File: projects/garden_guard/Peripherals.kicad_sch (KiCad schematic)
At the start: 13 parts, among them J1 Conn_02x05_Odd_Even, J6 Conn_02x06_Odd_Even, J8 Conn_02x01, J9 Conn_02x01, U10 DMN2028USS-13, U11 DMN2028USS-13

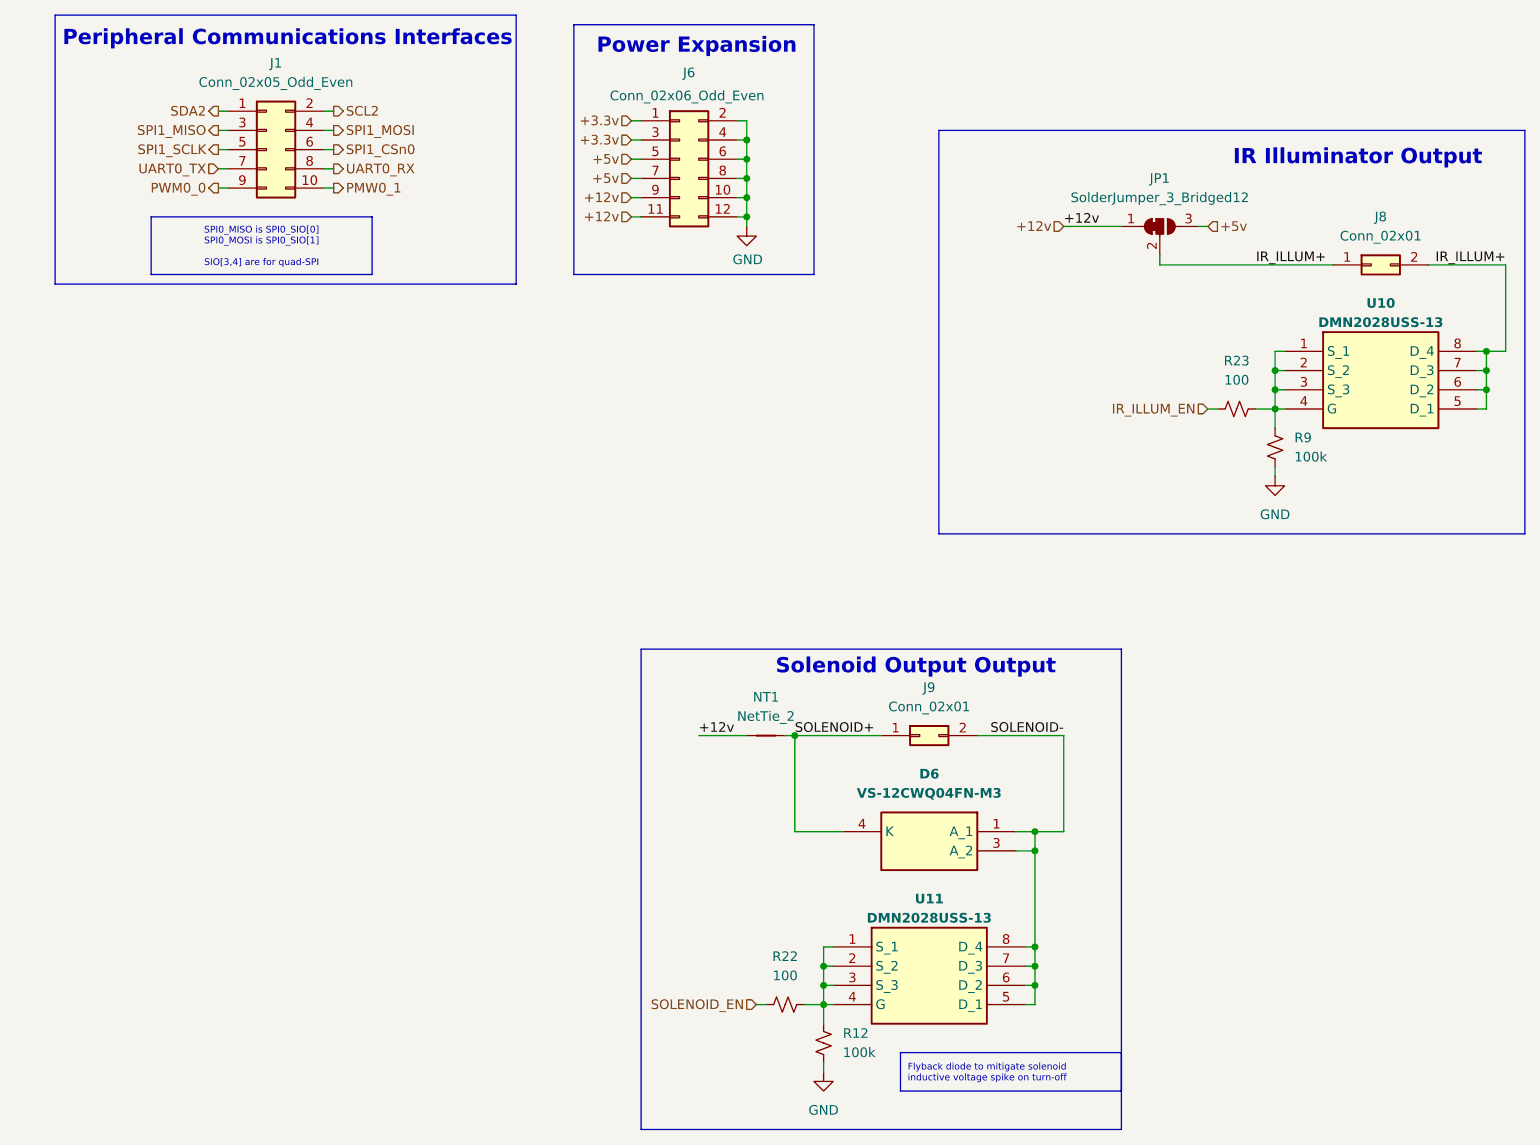
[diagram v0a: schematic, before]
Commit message: - Add all missing footprints - Add specific part numbers to each component in schematic
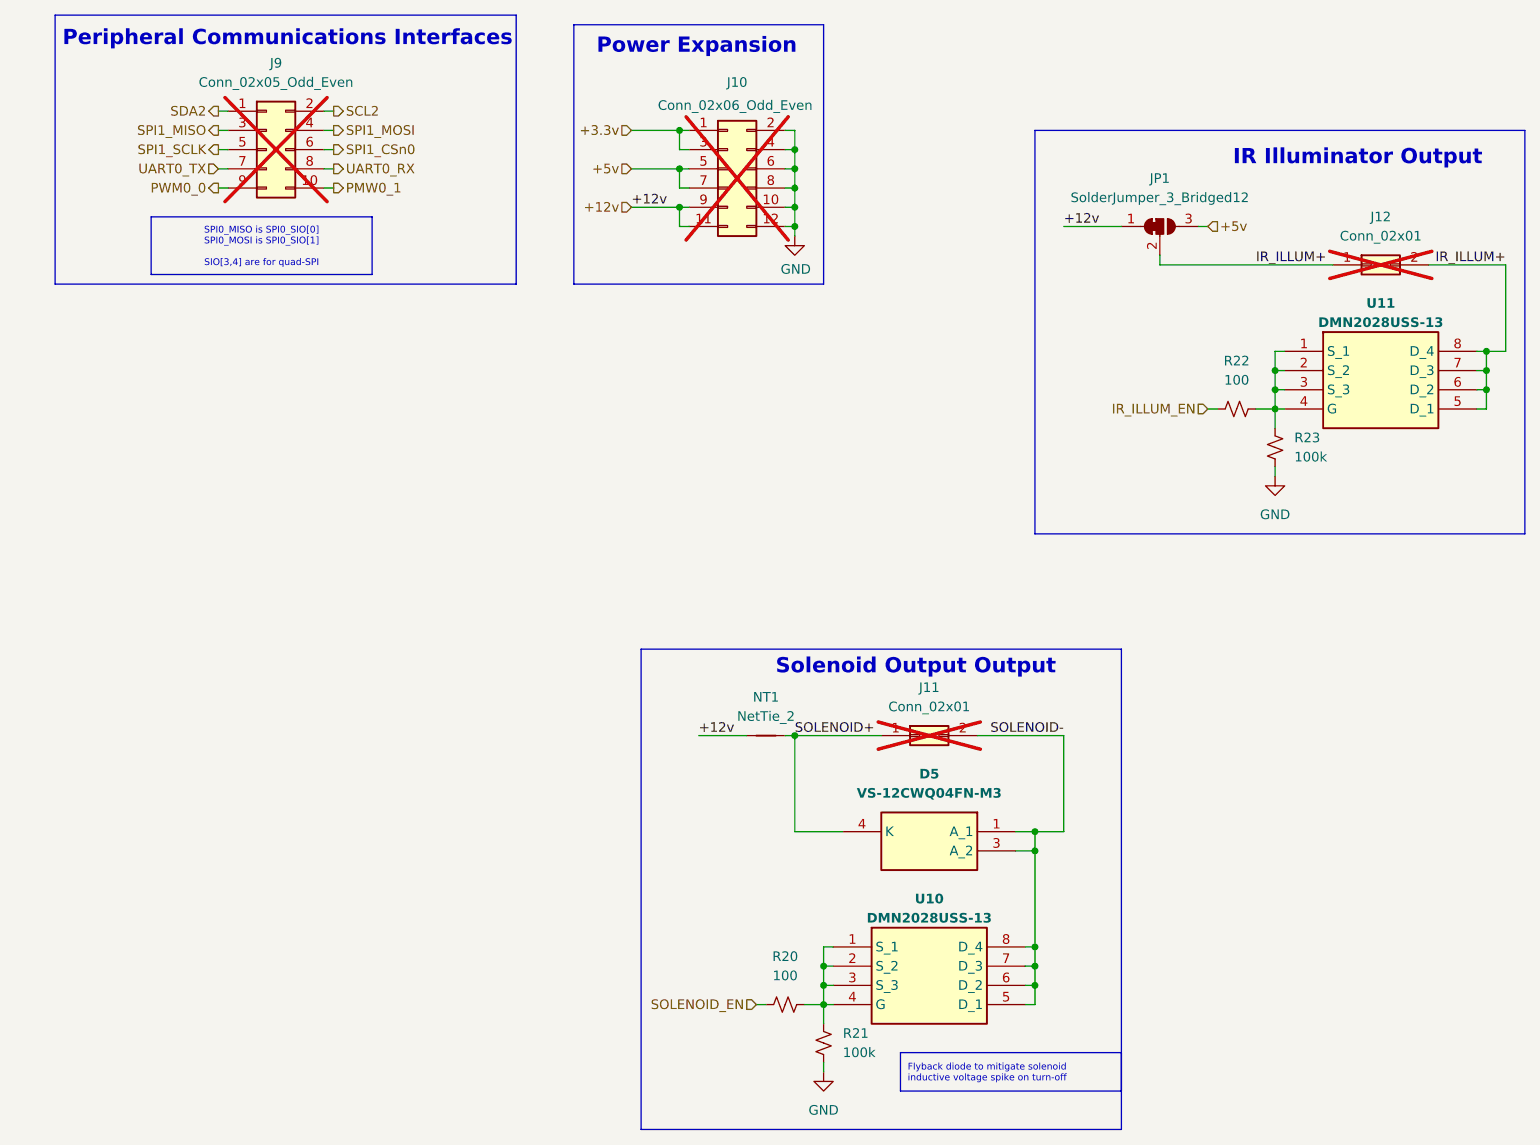
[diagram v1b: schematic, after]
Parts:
- removed J9: Conn_02x01, symbol Connector_Generic:Conn_02x01
- removed R9: 100k, symbol Device:R_Small_US
- added J11: Conn_02x01, Connector_PinHeader_2.54mm:PinHeader_1x02_P2.54mm_Vertical, symbol Connector_Generic:Conn_02x01
- added R23: 100k, Resistor_SMD:R_0603_1608Metric, symbol Device:R_Small_US
- J10: renamed from J6; footprint (none) -> Connector_PinHeader_2.54mm:PinHeader_2x06_P2.54mm_Vertical; now not fitted; now left out of the parts list
- J12: renamed from J8; footprint (none) -> Connector_PinHeader_2.54mm:PinHeader_1x02_P2.54mm_Vertical; now not fitted; now left out of the parts list
- J9: renamed from J1; footprint (none) -> Connector_PinHeader_2.54mm:PinHeader_2x05_P2.54mm_Vertical; now not fitted; now left out of the parts list
- JP1: footprint (none) -> Jumper:SolderJumper-3_P1.3mm_Bridged12_RoundedPad1.0x1.5mm
- NT1: footprint (none) -> NetTie:NetTie-2_SMD_Pad0.5mm
- R20: renamed from R22; footprint (none) -> Resistor_SMD:R_0603_1608Metric
- R21: renamed from R12; footprint (none) -> Resistor_SMD:R_0603_1608Metric; MPN (none) -> RC0603FR-07100KL; Mfr (none) -> YAGEO
- R22: renamed from R23; footprint (none) -> Resistor_SMD:R_0603_1608Metric
- renumbered D6 to D5, U11 to U10, U10 to U11
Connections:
- net GND: now also R23.2
- net SOLENOID+: now also J11.1 (Pin_1)
- net SOLENOID-: now also J11.2 (Pin_2)
- net at R22.2, U11.1 (S_1), U11.2 (S_2)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: now also R23.1

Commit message: - Find part numbers for CM5 parts - Minor CM5 symbol, footprint adjustments - Move to uniform small resistor and capacitor symbols - Add *lck to .gitignore
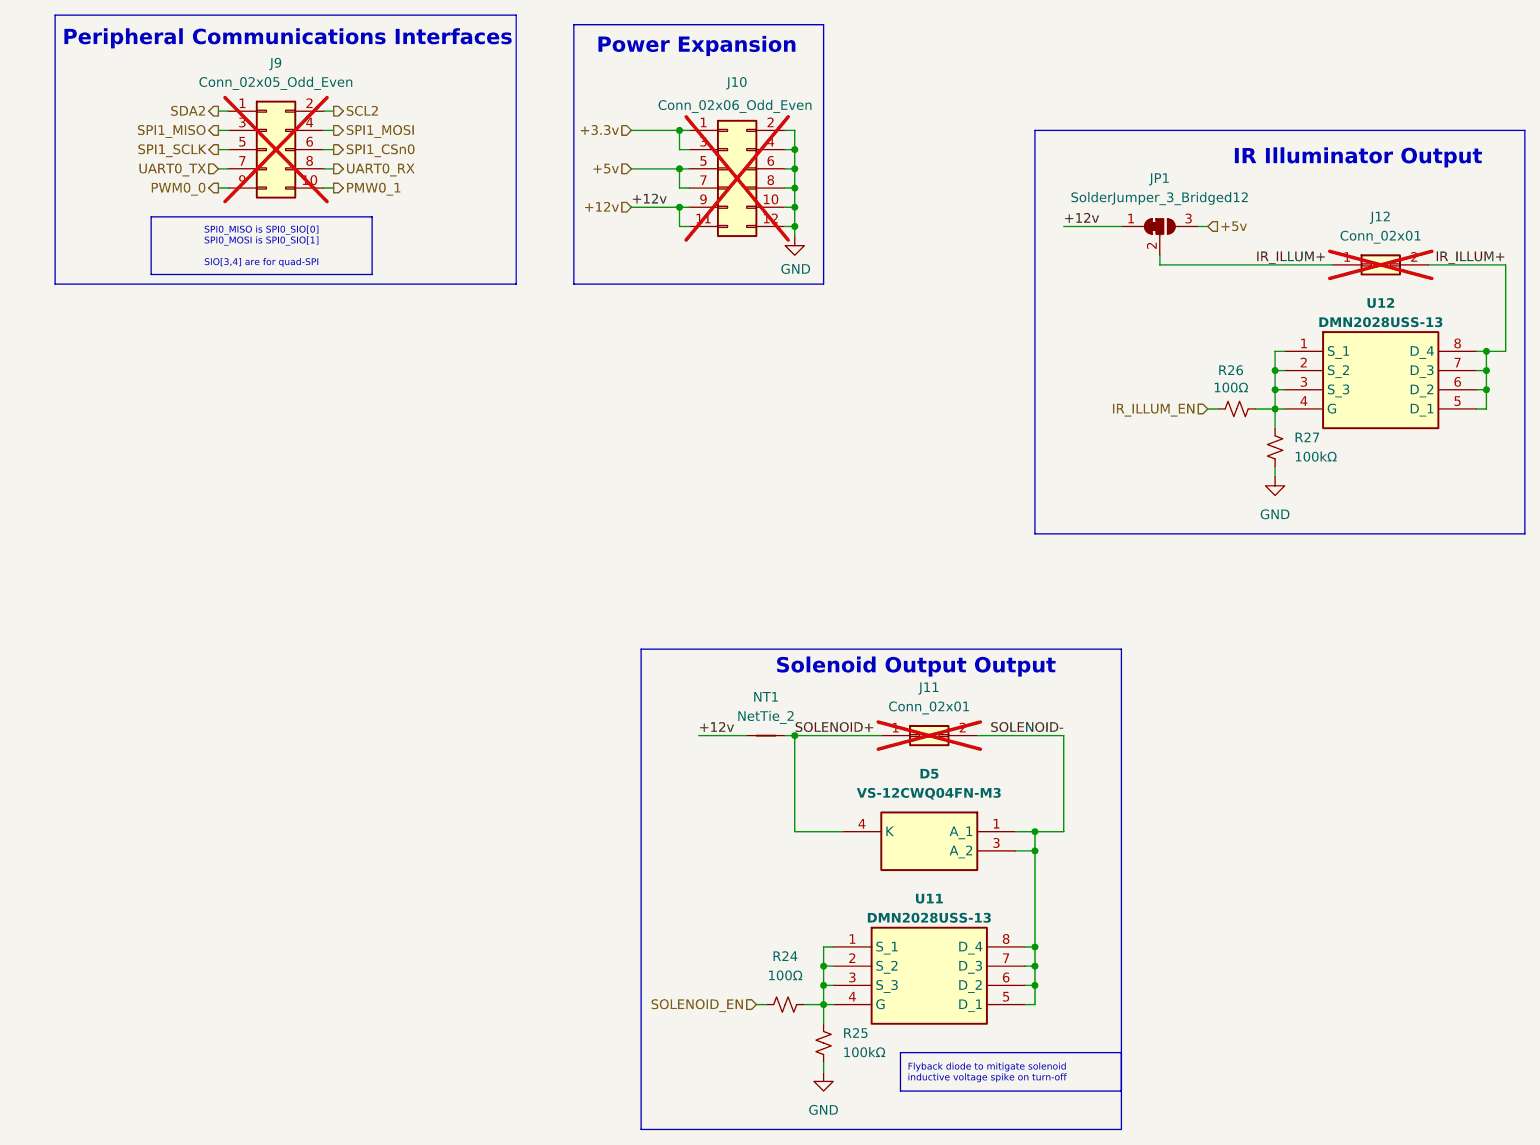
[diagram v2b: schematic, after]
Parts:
- removed R22: 100, Resistor_SMD:R_0603_1608Metric, symbol Device:R_Small_US
- removed R23: 100k, Resistor_SMD:R_0603_1608Metric, symbol Device:R_Small_US
- added R26: 100Ω, Resistor_SMD:R_0603_1608Metric, symbol Device:R_Small_US
- added R27: 100kΩ, Resistor_SMD:R_0603_1608Metric, symbol Device:R_Small_US
- D5: MPN (none) -> VS-12CWQ04FN-M3; Mfr (none) -> Vishay
- R24: renamed from R20; value 100 -> 100Ω; MPN (none) -> RC0603FR-07100RL; Mfr (none) -> YAGEO; Power (none) -> 1/10W; Tolerance (none) -> 1%
- R25: renamed from R21; value 100k -> 100kΩ
- U11: renamed from U10; MPN (none) -> DMN2028USS-13; Mfr (none) -> Diodes Incorporated
- U12: renamed from U11; MPN (none) -> DMN2028USS-13; Mfr (none) -> Diodes Incorporated
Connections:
- net GND: now also R27.2
- net IR_ILLUM_EN: now also R26.2
- net at U12.1 (S_1), U12.2 (S_2), U12.3 (S_3)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: now also R26.1, R27.1
